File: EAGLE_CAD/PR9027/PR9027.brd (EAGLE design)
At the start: 65.9 x 66 mm, 60 parts, among them SW1 C&K_PTS645

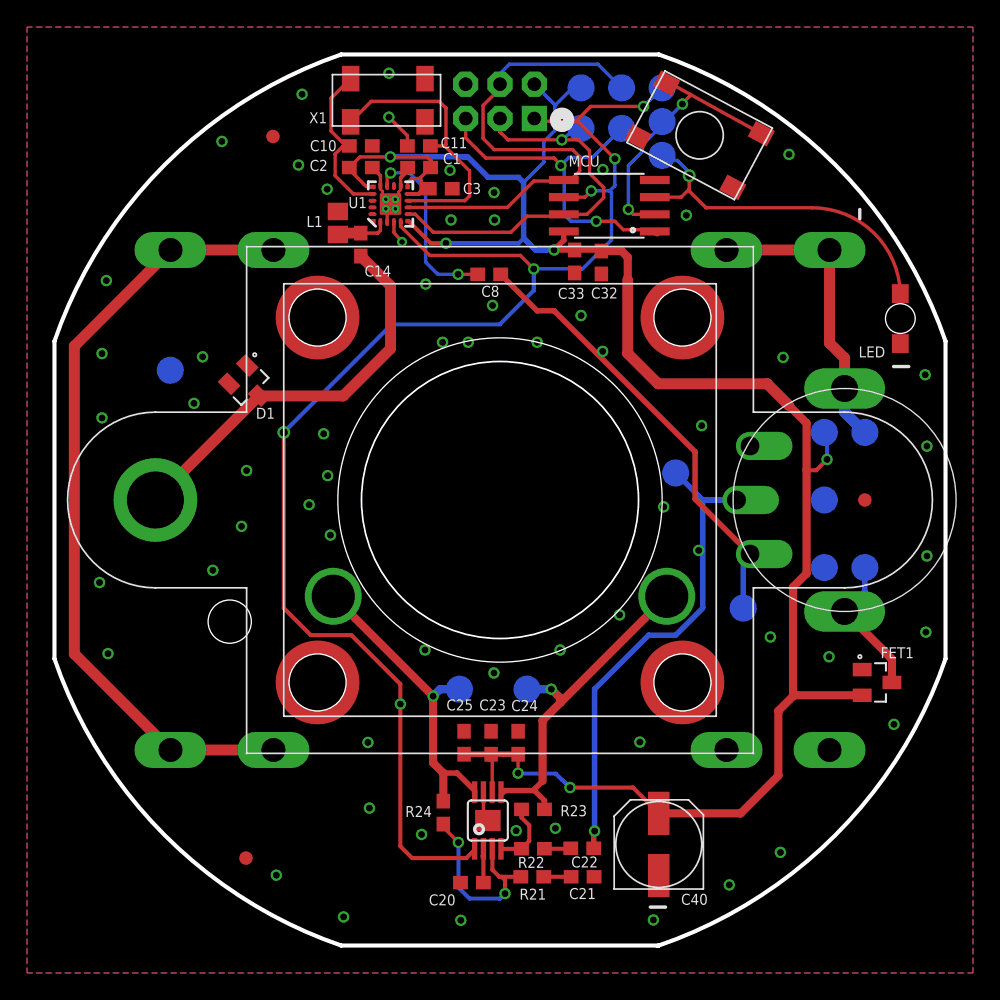
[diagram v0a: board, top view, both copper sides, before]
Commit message: Speaker hole ID & Pem Nuts
Updated the speaker hole ID to 11.25mm
Updated all pem nut pad sizes to 6.6mm
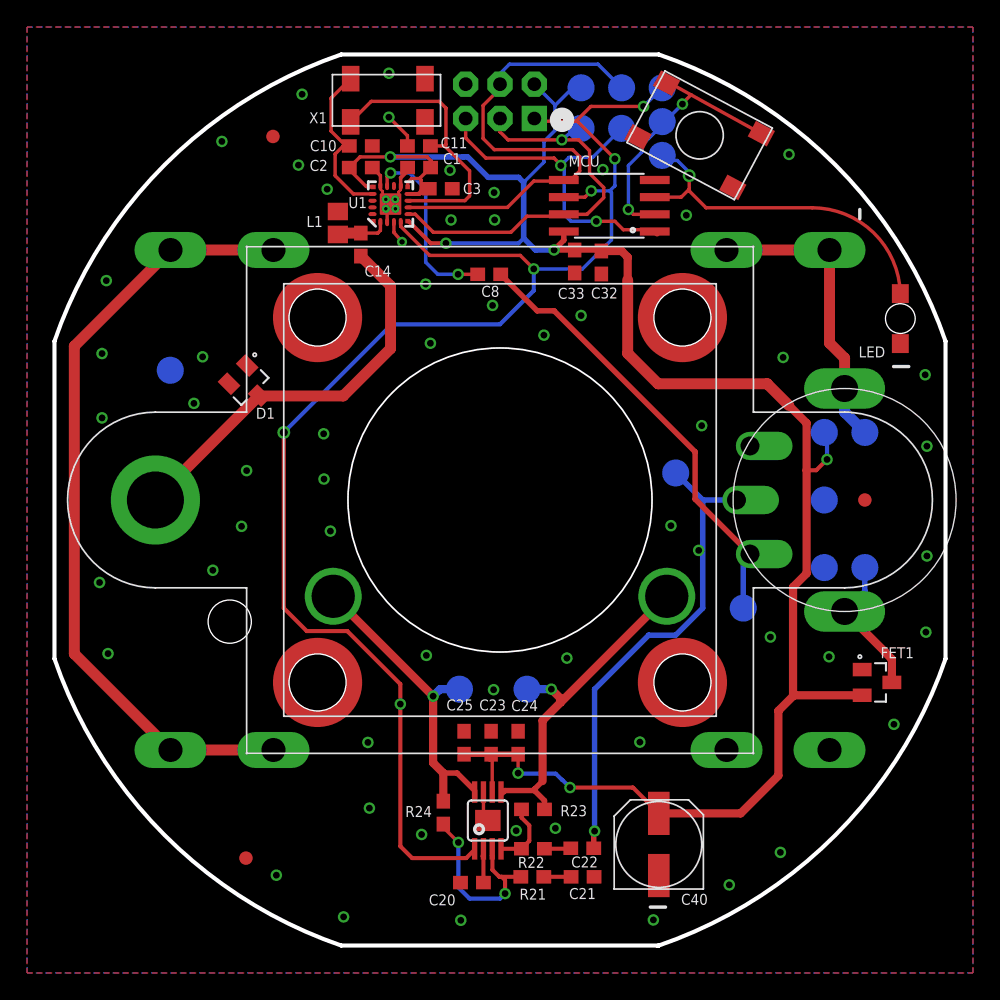
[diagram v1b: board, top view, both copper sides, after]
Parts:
- SPKR_PLACE: value (none) -> PR2024_SPKR_SMD
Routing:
- net GND: vias 66 -> 62
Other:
- outline, holes or cut-outs redrawn
- board text added: ">Partname Born in Brooklyn http://thepublicrad.io"
- board text removed: "PR9026 Born in Brooklyn http://thepublicrad.io"
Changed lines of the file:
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@@
 <?xml version="1.0" encoding="utf-8"?>
 <!DOCTYPE eagle SYSTEM "eagle.dtd">
-<eagle version="7.7.0">
+<eagle version="6.6.0">
 <drawing>
 <settings>
@@
 <setting verticaltext="up"/>
 </settings>
-<grid distance="0.5" unitdist="mm" unit="mm" style="dots" multiple="1" display="yes" altdistance="0.1" altunitdist="mm" altunit="mm"/>
+<grid distance="0.1" unitdist="mm" unit="mm" style="dots" multiple="1" display="yes" altdistance="0.1" altunitdist="mm" altunit="mm"/>
 <layers>
 <layer number="1" name="Top" color="4" fill="1" visible="yes" active="yes"/>
@@
 <rectangle x1="35.7111" y1="10.3543" x2="35.7873" y2="10.3797" layer="26" rot="R90"/>
 <rectangle x1="35.6857" y1="10.2781" x2="35.8635" y2="10.3035" layer="26" rot="R90"/>
-<text x="65.25" y="35" size="0.8128" layer="26" font="vector" ratio="22" rot="MR270" align="center">PR9026
+<text x="65.25" y="35" size="0.8128" layer="26" font="vector" ratio="22" rot="MR270" align="center">&gt;Partname
 Born in Brooklyn
 http://thepublicrad.io</text>
@@
 <wire x1="46.125" y1="4.875" x2="47.25" y2="4.875" width="0.254" layer="21"/>
 <text x="20.875" y="62.875" size="0.8128" layer="25" font="vector" ratio="18">X1</text>
-<circle x="35" y="35" radius="12" width="0.01" layer="20"/>
 </plain>
 <attributes>
@@
 <pass name="Default">
 <param name="RoutingGrid" value="50mil"/>
-<param name="AutoGrid" value="1"/>
-<param name="Efforts" value="0"/>
-<param name="TopRouterVariant" value="1"/>
 <param name="tpViaShape" value="round"/>
 <param name="PrefDir.1" value="|"/>
@@
 <attribute name="MFG_PN" value="AO3435" x="62.9" y="21.5" size="1.778" layer="27" display="off"/>
 </element>
-<element name="SPKR_PLACE" library="PR_Parts_Library" package="PR2024_SPKR_PLACE(SMD)" value="" x="35" y="35" locked="yes"/>
+<element name="SPKR_PLACE" library="PR_Parts_Library" package="PR2024_SPKR_PLACE(SMD)" value="PR2024_SPKR_SMD" x="35" y="35" locked="yes"/>
 <element name="T14" library="PR_Parts_Library" package="TP20R" value="" x="62" y="30" smashed="yes" rot="MR0">
 <attribute name="NAME" x="62.3936" y="31.5416" size="0.6096" layer="26" font="vector" ratio="16" rot="MR0"/>
@@
 <contactref element="C32" pad="2"/>
 <via x="25.225" y="17.06" extent="1-16" drill="0.5"/>
-<via x="42.6" y="46" extent="1-16" drill="0.5"/>
 <contactref element="FET1" pad="1"/>
 <via x="26.55" y="56.55" extent="1-16" drill="0.254" alwaysstop="yes"/>
@@
 <via x="27.75" y="54.1" extent="1-16" drill="0.4"/>
 <via x="29.5" y="50.975" extent="1-16" drill="0.5"/>
-<via x="20.875" y="34.65" extent="1-16" drill="0.5"/>
-<via x="32.65" y="46.675" extent="1-16" drill="0.5"/>
+<via x="21.975" y="36.55" extent="1-16" drill="0.5"/>
 <via x="13.75" y="29.8" extent="1-16" drill="0.5"/>
 <via x="22.21" y="58" extent="1-16" drill="0.5"/>
@@
 <wire x1="27.15" y1="54.8" x2="27.75" y2="54.1" width="0.254" layer="1"/>
 <via x="45.35" y="17.085" extent="1-16" drill="0.5"/>
-<via x="47.1125" y="34.495" extent="1-16" drill="0.5"/>
 <via x="49.925" y="40.5" extent="1-16" drill="0.5"/>
 <via x="55.95" y="45.55" extent="1-16" drill="0.5"/>
@@
 <contactref element="LED" pad="P$2"/>
 <via x="66.5925" y="30.85875" extent="1-16" drill="0.5"/>
-<via x="34.55" y="22.2" extent="1-16" drill="0.5"/>
 <via x="5.9925" y="23.6325" extent="1-16" drill="0.5"/>
 <via x="5.3675" y="28.895" extent="1-16" drill="0.5"/>
@@
 <wire x1="26.65" y1="55.565" x2="26.65" y2="56.45" width="0.254" layer="1"/>
 <wire x1="26.65" y1="56.45" x2="26.55" y2="56.55" width="0.254" layer="1"/>
-<via x="29.45" y="23.9" extent="1-16" drill="0.5"/>
-<via x="39.45" y="23.9" extent="1-16" drill="0.5"/>
-<via x="22.25" y="36.8" extent="1-16" drill="0.5"/>
-<via x="22.45" y="32.4" extent="1-16" drill="0.5"/>
 <via x="21.95" y="39.9" extent="1-16" drill="0.5"/>
-<via x="37.75" y="46.675" extent="1-16" drill="0.5"/>
-<via x="30.75" y="46.675" extent="1-16" drill="0.5"/>
 <wire x1="27.65" y1="58.235" x2="27.65" y2="58.85" width="0.254" layer="1"/>
 <wire x1="27.65" y1="58.85" x2="28.16" y2="59.36" width="0.3048" layer="1"/>
@@
 <via x="29.2" y="10.25" extent="1-16" drill="0.5"/>
 <via x="42.6125" y="59.45" extent="1-16" drill="0.5"/>
-<via x="43.85" y="26.5" extent="1-16" drill="0.5"/>
+<via x="34.525" y="20.96" extent="1-16" drill="0.5"/>
+<via x="38.25" y="47.2" extent="1-16" drill="0.5"/>
+<via x="29.85" y="46.6" extent="1-16" drill="0.5"/>
+<via x="47.65" y="33.1" extent="1-16" drill="0.5"/>
+<via x="39.95" y="23.3" extent="1-16" drill="0.5"/>
+<via x="29.55" y="23.5" extent="1-16" drill="0.5"/>
+<via x="22.45" y="32.7" extent="1-16" drill="0.5"/>
 </signal>
 <signal name="N$1">
@@
 <wire x1="37.74" y1="63.03" x2="37.54" y2="63.23" width="0.254" layer="1"/>
 <wire x1="27.625" y1="19.9" x2="27.625" y2="21.375" width="0.3048" layer="1"/>
-<wire x1="27.625" y1="21.375" x2="24" y2="25" width="0.3048" layer="1"/>
-<wire x1="24" y1="25" x2="21" y2="25" width="0.3048" layer="1"/>
-<wire x1="21" y1="25" x2="19" y2="27" width="0.3048" layer="1"/>
+<wire x1="27.625" y1="21.375" x2="23.7" y2="25.3" width="0.3048" layer="1"/>
 <wire x1="19" y1="27" x2="19" y2="40" width="0.3048" layer="1"/>
 <via x="19" y="40" extent="1-16" drill="0.6"/>
@@
 <wire x1="35" y1="48" x2="37.5" y2="50.5" width="0.3048" layer="16"/>
 <wire x1="37.5" y1="50.5" x2="37.5" y2="52.1" width="0.3048" layer="16"/>
+<wire x1="23.7" y1="25.3" x2="20.7" y2="25.3" width="0.3048" layer="1"/>
+<wire x1="20.7" y1="25.3" x2="19" y2="27" width="0.3048" layer="1"/>
 </signal>
 <signal name="SCLK">

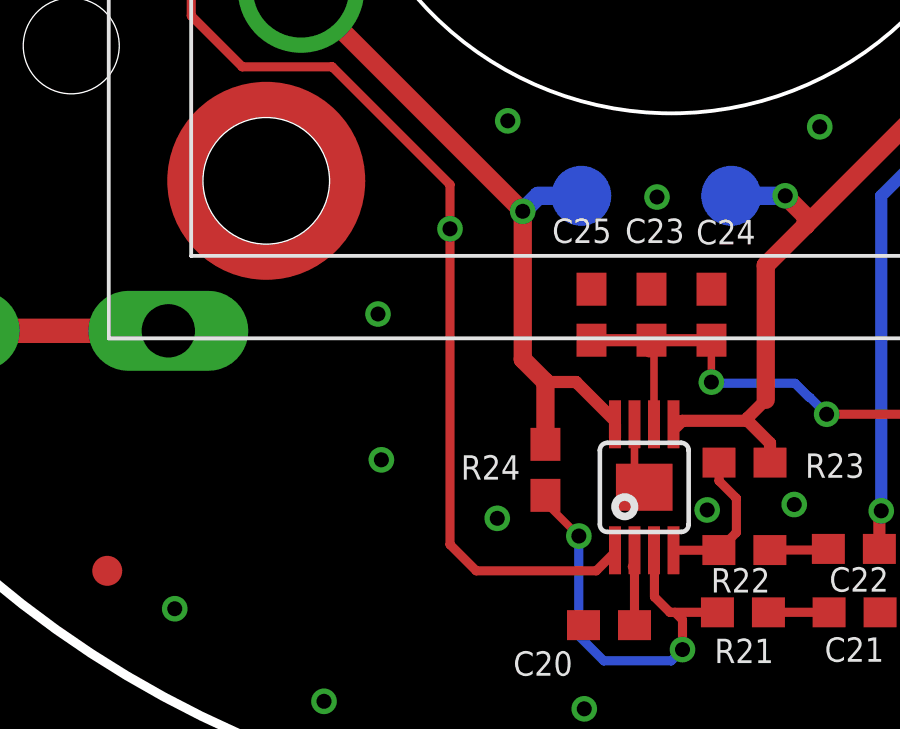
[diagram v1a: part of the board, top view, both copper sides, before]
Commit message: PEM Nuts & MFG#s
Updated PEM nut footprint OD to 6.6mm
Also updated the MFG part numbers on
- LED (HSMA-C265) AMBER!
- FET (AO3415A)
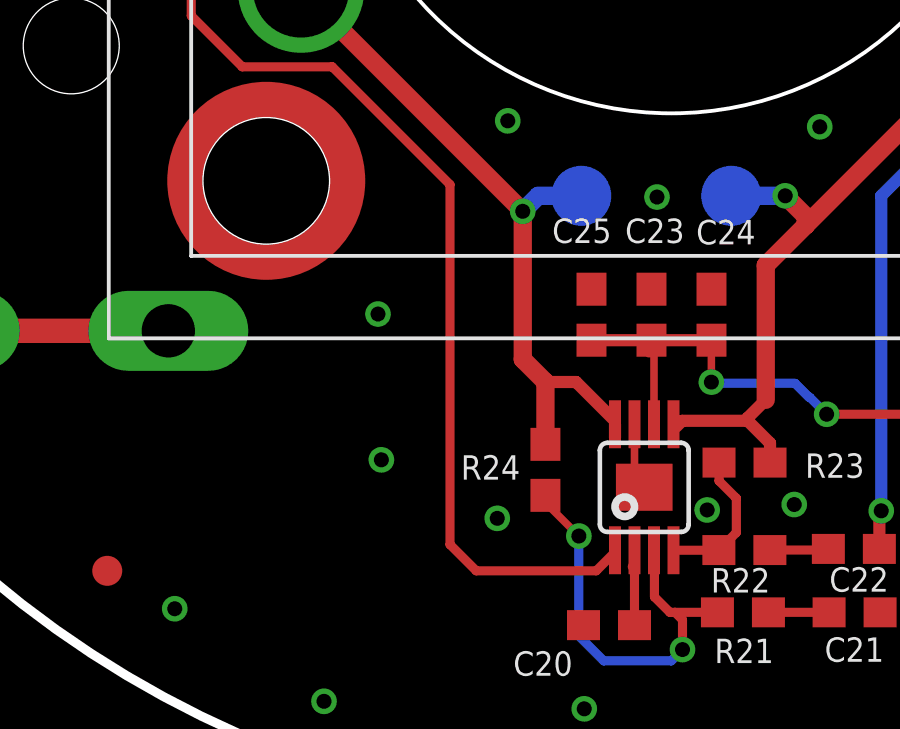
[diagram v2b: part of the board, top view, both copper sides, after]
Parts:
- LED: device PR_Parts_Library:HSMC-C265_REVERSE_MOUN_LED -> PR_Parts_Library:HSMA-C265_REVERSE_MOUN_LED
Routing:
- net !RST: vias 6 -> 5
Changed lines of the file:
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@@
 <setting verticaltext="up"/>
 </settings>
-<grid distance="0.1" unitdist="mm" unit="mm" style="dots" multiple="1" display="yes" altdistance="0.1" altunitdist="mm" altunit="mm"/>
+<grid distance="0.1" unitdist="mm" unit="mm" style="lines" multiple="1" display="yes" altdistance="0.1" altunitdist="mm" altunit="mm"/>
 <layers>
 <layer number="1" name="Top" color="4" fill="1" visible="yes" active="yes"/>
@@
 <attribute name="NAME" x="21.8745" y="56.013" size="0.8128" layer="25" font="vector" ratio="18" rot="R180"/>
 <attribute name="VALUE" x="24.397" y="54.484" size="0.4064" layer="27" rot="R90"/>
-<attribute name="MFG_PN" value="AISC-0805-R18J-T" x="23" y="55.5" size="1.778" layer="27" rot="R90" display="off"/>
+<attribute name="MFG_PN" value="AISC-0805-R18J-T
+" x="23" y="55.5" size="1.778" layer="27" rot="R90" display="off"/>
 <attribute name="CURRENT" value="400mA" x="23" y="55.5" size="1.778" layer="27" rot="R90" display="off"/>
 <attribute name="TOL" value="5%" x="23" y="55.5" size="1.778" layer="27" rot="R90" display="off"/>
@@
 <attribute name="NAME" x="65.6245" y="24.103" size="0.8128" layer="25" font="vector" ratio="18" rot="R180"/>
 <attribute name="VALUE" x="61.884" y="21.3095" size="0.4064" layer="27"/>
-<attribute name="MFG_PN" value="AO3435" x="62.9" y="21.5" size="1.778" layer="27" display="off"/>
+<attribute name="MFG_PN" value="AO3415A" x="62.9" y="21.5" size="1.778" layer="27" display="off"/>
 </element>
 <element name="SPKR_PLACE" library="PR_Parts_Library" package="PR2024_SPKR_PLACE(SMD)" value="PR2024_SPKR_SMD" x="35" y="35" locked="yes"/>
@@
 </element>
 <element name="U$1" library="PR_Parts_Library" package="PR_LOGO" value="" x="35" y="9" rot="MR0"/>
-<element name="LED" library="PR_Parts_Library" package="HSMC-C265_REVERSE_MOUN_LED" value="HSMC-C265_REVERSE_MOUNT_LED" x="64.625" y="48.425" smashed="yes" rot="R270">
+<element name="LED" library="PR_Parts_Library" package="HSMA-C265_REVERSE_MOUN_LED" value="HSMC-C265_REVERSE_MOUNT_LED" x="64.625" y="48.425" smashed="yes" rot="R270">
 <attribute name="NAME" x="63.5025" y="46.3625" size="0.8128" layer="25" font="vector" ratio="18" rot="R180"/>
 <attribute name="VALUE" x="63.355" y="45.885" size="1.27" layer="27"/>
-<attribute name="MFG_PN" value="HSMC-C265" x="64.625" y="48.425" size="1.778" layer="27" rot="R270" display="off"/>
+<attribute name="MFG_PN" value="HSMA-C265" x="64.625" y="48.425" size="1.778" layer="27" rot="R270" display="off"/>
 </element>
 <element name="U$2" library="PR_Parts_Library" package="PEM_SMT" value="PEM_SMT" x="21.5" y="48.5" locked="yes"/>
@@
 <wire x1="32.5" y1="8.5" x2="28.5" y2="8.5" width="0.3048" layer="1"/>
 <wire x1="28.5" y1="8.5" x2="27.625" y2="9.375" width="0.3048" layer="1"/>
-<wire x1="27.625" y1="9.375" x2="27.625" y2="19.9" width="0.3048" layer="1"/>
-<via x="27.625" y="19.9" extent="1-16" drill="0.5"/>
+<wire x1="27.625" y1="9.375" x2="27.625" y2="21.375" width="0.3048" layer="1"/>
 <wire x1="43.125" y1="57.875" x2="43.48169375" y2="58.23169375" width="0.254" layer="16"/>
 <wire x1="43.48169375" y1="58.23169375" x2="43.5" y2="58.2758875" width="0.254" layer="16" curve="45"/>
@@
 <wire x1="40.625" y1="63.03" x2="37.74" y2="63.03" width="0.254" layer="1"/>
 <wire x1="37.74" y1="63.03" x2="37.54" y2="63.23" width="0.254" layer="1"/>
-<wire x1="27.625" y1="19.9" x2="27.625" y2="21.375" width="0.3048" layer="1"/>
 <wire x1="27.625" y1="21.375" x2="23.7" y2="25.3" width="0.3048" layer="1"/>
 <wire x1="19" y1="27" x2="19" y2="40" width="0.3048" layer="1"/>
